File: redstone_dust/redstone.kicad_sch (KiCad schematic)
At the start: 71 parts, among them J1 1x4_Pogo, J2 1x4_Pogo, J3 1x4_Pogo, J4 1x4_Pogo, J5 1x4_Pogo, J6 1x4_Pogo, J7 1x4_Pogo, J8 1x4_Pogo, J9 2.54mm_ProgrammingPin, Q1 BC108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

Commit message: add dip switch to schematic, todo update pcb design
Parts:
- added SW2: SW_DIP_x01, symbol Switch:SW_DIP_x01
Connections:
- net E_RX: now also U1.30 (GPIO19); no longer U1.29 (GPIO18)
- net E_TX: now also U1.31 (GPIO20); no longer U1.30 (GPIO19)
- net GND: now also SW2.2
- new net: SW2.1, U1.29 (GPIO18)
- no-connect marks 31 -> 30
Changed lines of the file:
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@@
 	)
 	(junction
+		(at 176.53 132.08)
+		(diameter 0)
+		(color 0 0 0 0)
+	)
+	(junction
 		(at 257.81 87.63)
 		(diameter 0)
@@
 	)
 	(no_connect
-		(at 128.27 137.16)
-	)
-	(no_connect
 		(at 270.51 72.39)
 	)
@@
 	(wire
 		(pts
+			(xy 152.4 132.08) (xy 176.53 132.08)
+		)
+		(stroke
+			(width 0)
+			(type default)
+		)
+	)
+	(wire
+		(pts
 			(xy 171.45 64.77) (xy 171.45 129.54)
 		)
@@
 	(wire
 		(pts
-			(xy 176.53 80.01) (xy 176.53 161.29)
+			(xy 176.53 80.01) (xy 176.53 132.08)
 		)
 		(stroke
@@
 	(wire
 		(pts
+			(xy 128.27 132.08) (xy 137.16 132.08)
+		)
+		(stroke
+			(width 0)
+			(type default)
+		)
+	)
+	(wire
+		(pts
 			(xy 186.69 66.04) (xy 196.85 66.04)
 		)
@@
 	(wire
 		(pts
+			(xy 176.53 132.08) (xy 176.53 161.29)
+		)
+		(stroke
+			(width 0)
+			(type default)
+			(color 0 0 0 1)
+		)
+	)
+	(wire
+		(pts
 			(xy 168.91 71.12) (xy 181.61 71.12)
 		)
@@
 	)
 	(label "E_RX"
-		(at 128.27 132.08 0)
+		(at 128.27 134.62 0)
 		(effects
 			(font
@@
 	)
 	(label "E_TX"
-		(at 128.27 134.62 0)
+		(at 128.27 137.16 0)
 		(effects
 			(font
@@
 					(unit 1)
 				)
+			)
+		)
+	)
+	(symbol
+		(lib_id "Switch:SW_DIP_x01")
+		(at 144.78 132.08 0)
+		(unit 1)
+		(exclude_from_sim no)
+		(in_bom yes)
+		(on_board yes)
+		(dnp no)
+		(property "Reference" "SW2"
+			(at 144.78 124.46 0)
+			(effects
+				(font
+					(size 1.27 1.27)
+				)
+			)
+		)
+		(property "Value" "SW_DIP_x01"
+			(at 144.78 127 0)
+			(effects
+				(font
+					(size 1.27 1.27)
+				)
+			)
+		)
+		(property "Footprint" ""
+			(at 144.78 132.08 0)
+			(effects
+				(font
+					(size 1.27 1.27)
+				)
+				(hide yes)
+			)
+		)
+		(property "Datasheet" "~"
+			(at 144.78 132.08 0)
+			(effects
+				(font
+					(size 1.27 1.27)
+				)
+				(hide yes)
+			)
+		)
+		(property "Description" "1x DIP Switch, Single Pole Single Throw (SPST) switch, small symbol"
+			(at 144.78 132.08 0)
+			(effects
+				(font
+					(size 1.27 1.27)
+				)
+				(hide yes)
+			)
+		)
+		(pin "1"
+		)
+		(pin "2"
+		)
+		(instances
+			(project ""
+				(path "/bc70a981-f687-4b66-9b14-62168cfa8164"
+					(reference "SW2")
+					(unit 1)
+				)

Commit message: remove dip switch, cannot find one that fits in board space
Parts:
- removed SW2: SW_DIP_x01, symbol Switch:SW_DIP_x01
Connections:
- net E_RX: now also U1.29 (GPIO18); no longer U1.30 (GPIO19)
- net E_TX: now also U1.30 (GPIO19); no longer U1.31 (GPIO20)
- no-connect marks 30 -> 31
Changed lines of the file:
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@@
 	)
 	(junction
-		(at 176.53 132.08)
-		(diameter 0)
-		(color 0 0 0 0)
-	)
-	(junction
 		(at 257.81 87.63)
 		(diameter 0)
@@
 	)
 	(no_connect
+		(at 128.27 137.16)
+	)
+	(no_connect
 		(at 77.47 93.98)
 	)
@@
 	(wire
 		(pts
-			(xy 152.4 132.08) (xy 176.53 132.08)
-		)
-		(stroke
-			(width 0)
-			(type default)
-		)
-	)
-	(wire
-		(pts
 			(xy 171.45 64.77) (xy 171.45 129.54)
 		)
@@
 	(wire
 		(pts
-			(xy 176.53 80.01) (xy 176.53 132.08)
-		)
-		(stroke
-			(width 0)
-			(type default)
-			(color 0 0 0 1)
-		)
-	)
-	(wire
-		(pts
 			(xy 196.85 30.48) (xy 207.01 30.48)
 		)
@@
 	(wire
 		(pts
-			(xy 128.27 132.08) (xy 137.16 132.08)
-		)
-		(stroke
-			(width 0)
-			(type default)
-		)
-	)
-	(wire
-		(pts
 			(xy 186.69 66.04) (xy 196.85 66.04)
 		)
@@
 	(wire
 		(pts
-			(xy 176.53 132.08) (xy 176.53 161.29)
+			(xy 176.53 80.01) (xy 176.53 161.29)
 		)
 		(stroke
@@
 	)
 	(label "E_RX"
-		(at 128.27 134.62 0)
+		(at 128.27 132.08 0)
 		(effects
 			(font
@@
 	)
 	(label "E_TX"
-		(at 128.27 137.16 0)
+		(at 128.27 134.62 0)
 		(effects
 			(font
@@
 					(unit 1)
 				)
-			)
-		)
-	)
-	(symbol
-		(lib_id "Switch:SW_DIP_x01")
-		(at 144.78 132.08 0)
-		(unit 1)
-		(exclude_from_sim no)
-		(in_bom yes)
-		(on_board yes)
-		(dnp no)
-		(property "Reference" "SW2"
-			(at 144.78 124.46 0)
-			(effects
-				(font
-					(size 1.27 1.27)
-				)
-			)
-		)
-		(property "Value" "SW_DIP_x01"
-			(at 144.78 127 0)
-			(effects
-				(font
-					(size 1.27 1.27)
-				)
-			)
-		)
-		(property "Footprint" ""
-			(at 144.78 132.08 0)
-			(effects
-				(font
-					(size 1.27 1.27)
-				)
-				(hide yes)
-			)
-		)
-		(property "Datasheet" "~"
-			(at 144.78 132.08 0)
-			(effects
-				(font
-					(size 1.27 1.27)
-				)
-				(hide yes)
-			)
-		)
-		(property "Description" "1x DIP Switch, Single Pole Single Throw (SPST) switch, small symbol"
-			(at 144.78 132.08 0)
-			(effects
-				(font
-					(size 1.27 1.27)
-				)
-				(hide yes)
-			)
-		)
-		(pin "1"
-		)
-		(pin "2"
-		)
-		(instances
-			(project ""
-				(path "/bc70a981-f687-4b66-9b14-62168cfa8164"
-					(reference "SW2")
-					(unit 1)
-				)

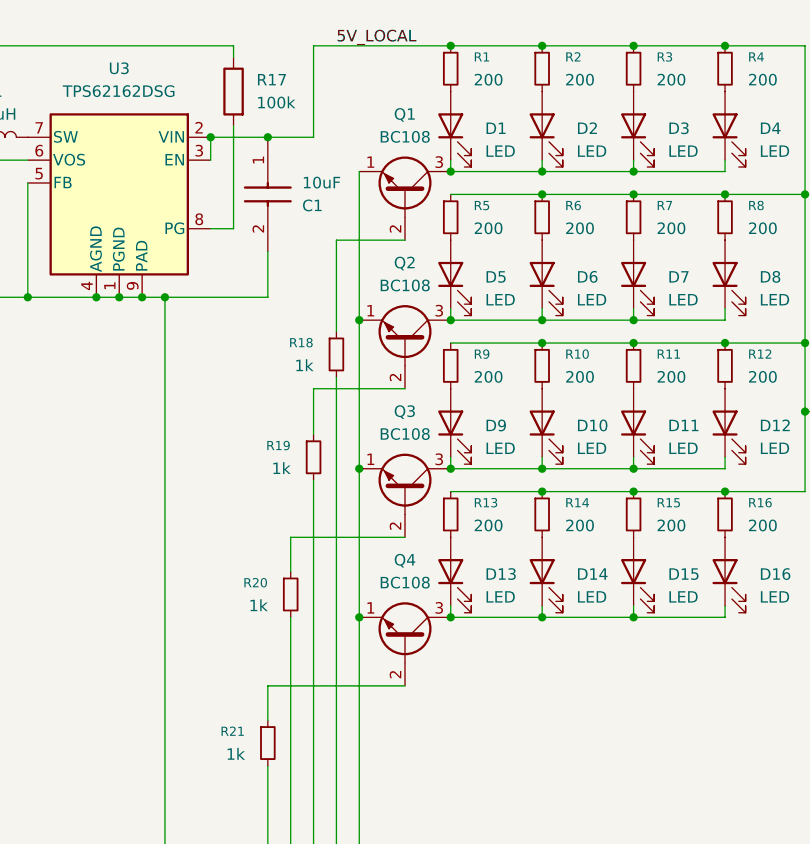
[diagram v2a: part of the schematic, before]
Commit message: switch redstone dust transistor to a much smaller one, todo switch transistors on other tiles as well
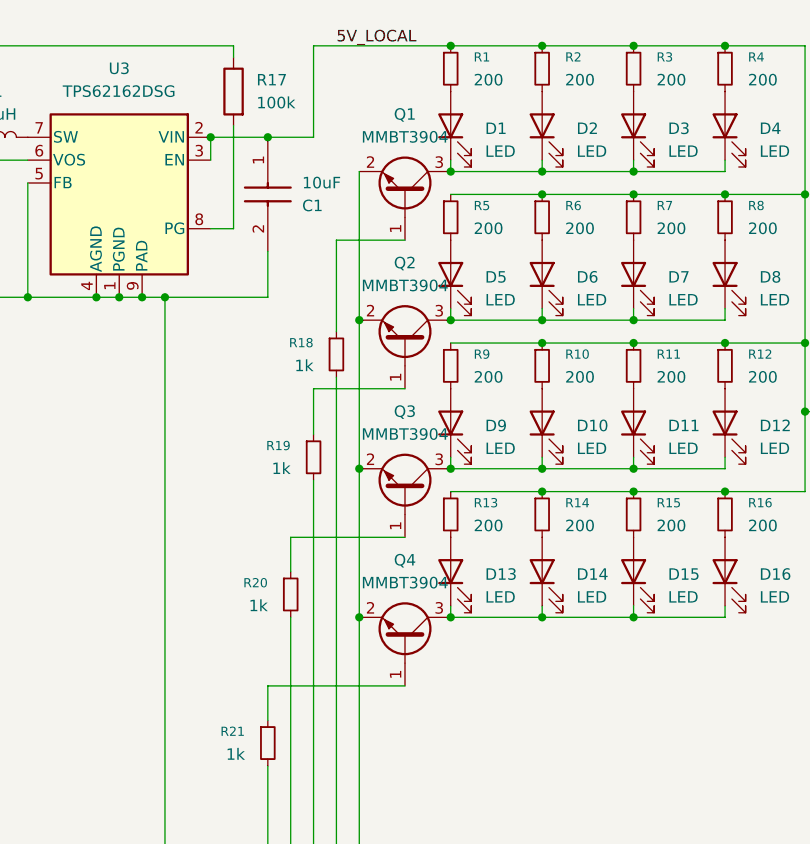
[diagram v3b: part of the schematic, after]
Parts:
- removed Q1, Q2, Q3, Q4: BC108, Package_TO_SOT_THT:TO-18-3, symbol Transistor_BJT:BC108
- added Q1, Q2, Q3, Q4: MMBT3904, Package_TO_SOT_SMD:SOT-23, symbol Transistor_BJT:MMBT3904
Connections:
- net GND: now also Q1.2 (E), Q2.2 (E), Q3.2 (E), Q4.2 (E)
- net at D1.1 (K), D2.1 (K), D3.1 (K)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: now also Q1.3 (C)
- net at R18.1: now also Q1.1 (B)
- net at R19.1: now also Q2.1 (B)
- net at D5.1 (K), D6.1 (K), D7.1 (K)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: now also Q2.3 (C)
- net at D13.1 (K), D14.1 (K), D15.1 (K)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: now also Q4.3 (C)
- net at R21.1: now also Q4.1 (B)
- net at D10.1 (K), D11.1 (K), D12.1 (K)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: now also Q3.3 (C)
- net at R20.1: now also Q3.1 (B)

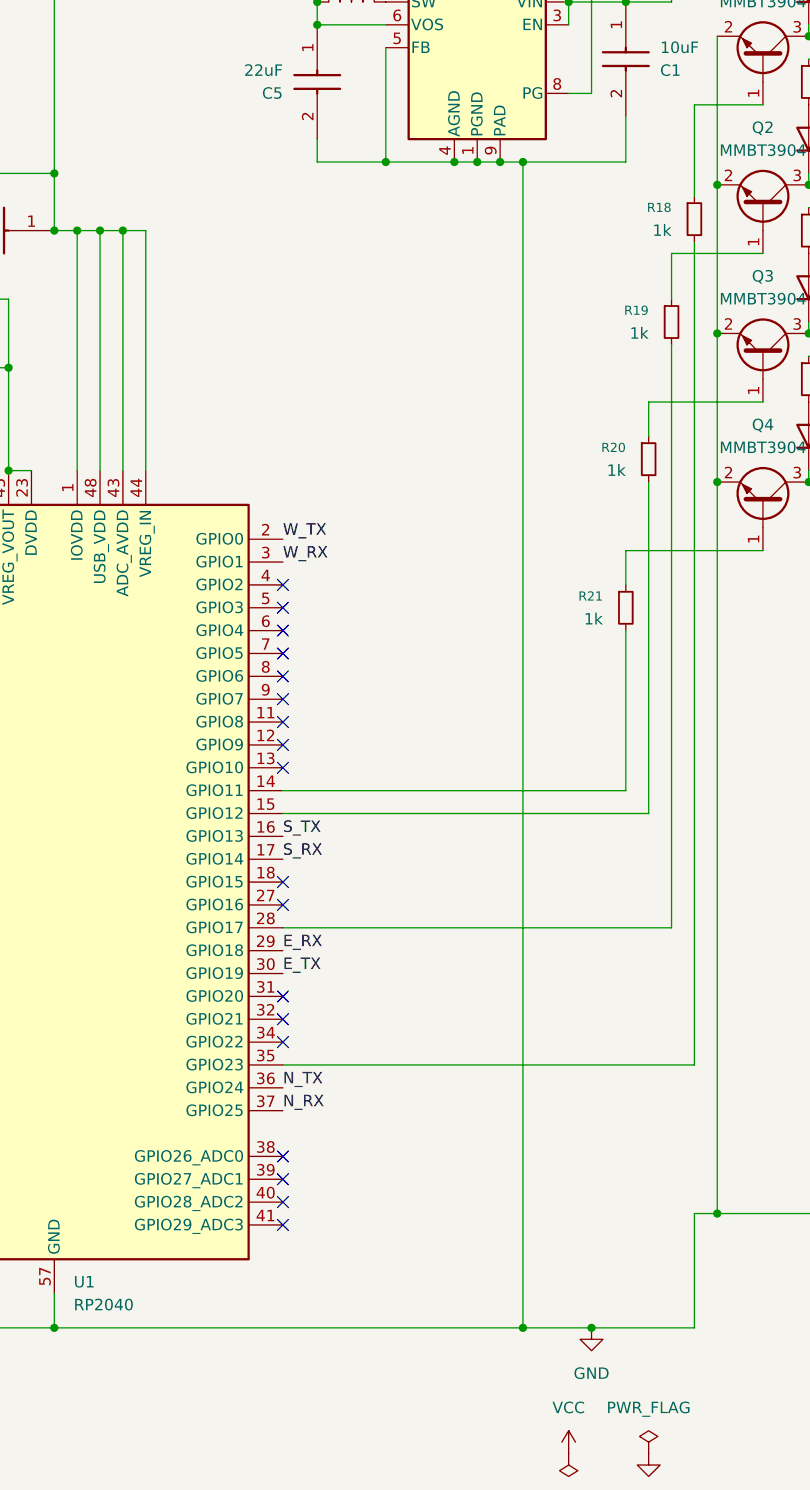
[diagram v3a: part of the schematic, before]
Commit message: move reset buttom and add dip switch
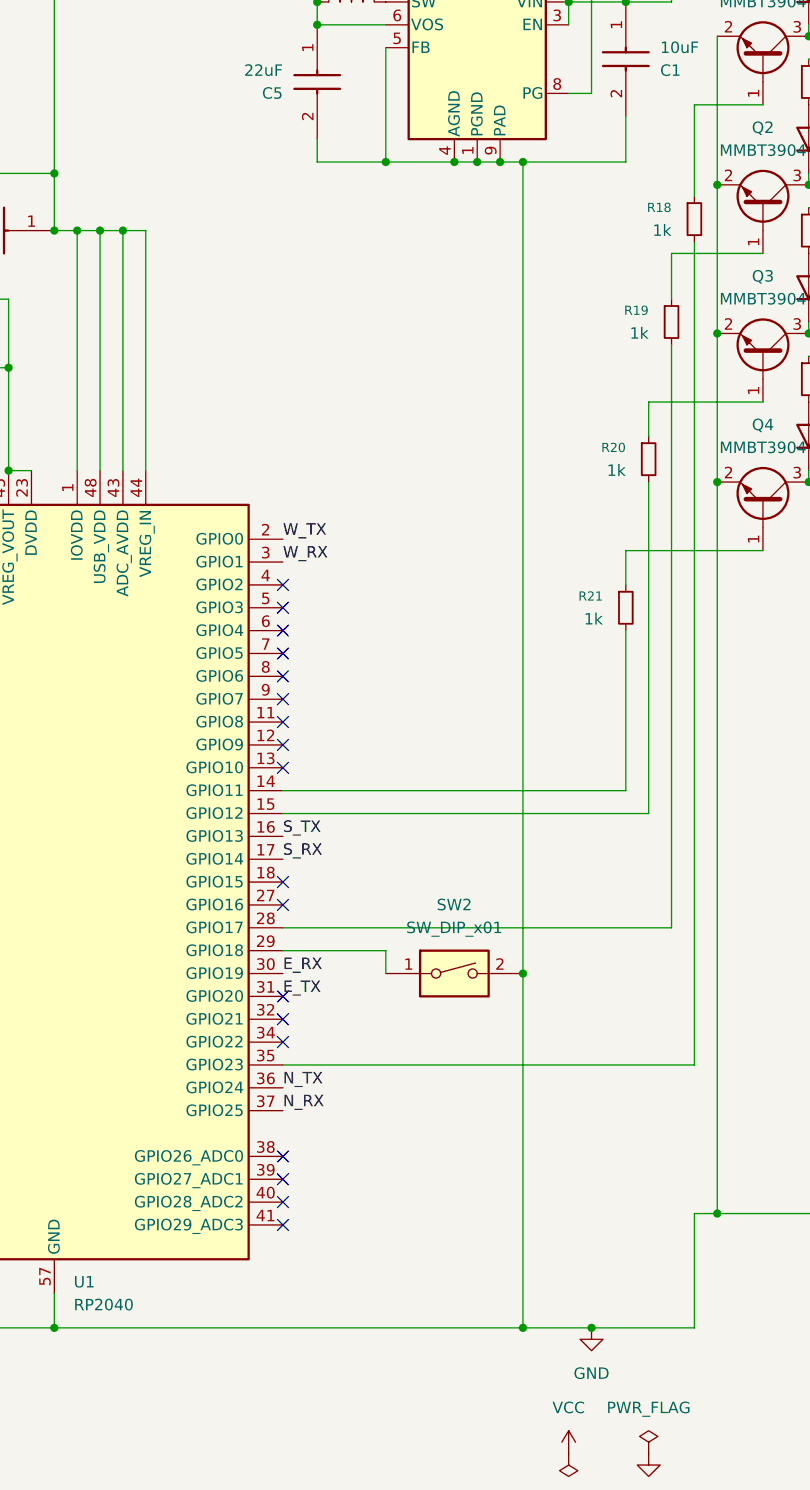
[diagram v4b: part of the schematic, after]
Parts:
- added SW2: SW_DIP_x01, SamacSys_Parts:416131160801, symbol Switch:SW_DIP_x01
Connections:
- net E_RX: now also U1.30 (GPIO19); no longer U1.29 (GPIO18)
- net E_TX: now also U1.31 (GPIO20); no longer U1.30 (GPIO19)
- net GND: now also SW2.2
- new net: SW2.1, U1.29 (GPIO18)
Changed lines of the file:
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@@
 	)
 	(junction
+		(at 154.94 134.62)
+		(diameter 0)
+		(color 0 0 0 0)
+	)
+	(junction
 		(at 247.65 21.59)
 		(diameter 0)
@@
 	(wire
 		(pts
+			(xy 139.7 132.08) (xy 139.7 134.62)
+		)
+		(stroke
+			(width 0)
+			(type default)
+		)
+	)
+	(wire
+		(pts
 			(xy 196.85 46.99) (xy 207.01 46.99)
 		)
@@
 	(wire
 		(pts
-			(xy 154.94 44.45) (xy 154.94 173.99)
+			(xy 154.94 44.45) (xy 154.94 134.62)
 		)
 		(stroke
@@
 	(wire
 		(pts
+			(xy 128.27 132.08) (xy 139.7 132.08)
+		)
+		(stroke
+			(width 0)
+			(type default)
+		)
+	)
+	(wire
+		(pts
 			(xy 152.4 44.45) (xy 154.94 44.45)
 		)
@@
 	(wire
 		(pts
+			(xy 154.94 134.62) (xy 154.94 173.99)
+		)
+		(stroke
+			(width 0)
+			(type default)
+			(color 0 0 0 1)
+		)
+	)
+	(wire
+		(pts
 			(xy 102.87 52.07) (xy 105.41 52.07)
 		)
@@
 	)
 	(label "E_RX"
-		(at 128.27 132.08 0)
+		(at 128.27 134.62 0)
 		(effects
 			(font
@@
 	)
 	(label "E_TX"
-		(at 128.27 134.62 0)
+		(at 128.27 137.16 0)
 		(effects
 			(font
@@
 					(unit 1)
 				)
+			)
+		)
+	)
+	(symbol
+		(lib_id "Switch:SW_DIP_x01")
+		(at 147.32 134.62 0)
+		(unit 1)
+		(exclude_from_sim no)
+		(in_bom yes)
+		(on_board yes)
+		(dnp no)
+		(fields_autoplaced yes)
+		(property "Reference" "SW2"
+			(at 147.32 127 0)
+			(effects
+				(font
+					(size 1.27 1.27)
+				)
+			)
+		)
+		(property "Value" "SW_DIP_x01"
+			(at 147.32 129.54 0)
+			(effects
+				(font
+					(size 1.27 1.27)
+				)
+			)
+		)
+		(property "Footprint" "SamacSys_Parts:416131160801"
+			(at 147.32 134.62 0)
+			(effects
+				(font
+					(size 1.27 1.27)
+				)
+				(hide yes)
+			)
+		)
+		(property "Datasheet" "~"
+			(at 147.32 134.62 0)
+			(effects
+				(font
+					(size 1.27 1.27)
+				)
+				(hide yes)
+			)
+		)
+		(property "Description" "1x DIP Switch, Single Pole Single Throw (SPST) switch, small symbol"
+			(at 147.32 134.62 0)
+			(effects
+				(font
+					(size 1.27 1.27)
+				)
+				(hide yes)
+			)
+		)
+		(pin "2"
+		)
+		(pin "1"
+		)
+		(instances
+			(project ""
+				(path "/bc70a981-f687-4b66-9b14-62168cfa8164"
+					(reference "SW2")
+					(unit 1)
+				)
